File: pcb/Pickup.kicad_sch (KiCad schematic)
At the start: 39 parts, among them IC1 MAX9924UAUB+, K1 AQY212EHAX, Q7 MMBT2222A, T1 SM-LP-5001E

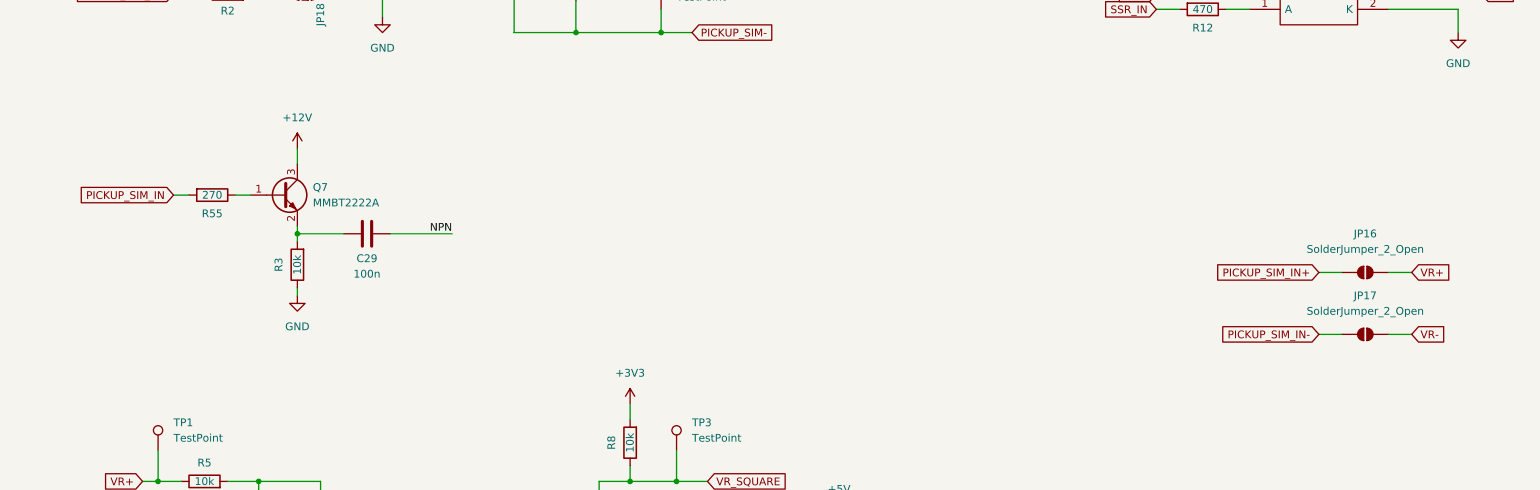
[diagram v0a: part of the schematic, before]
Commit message: simplified pickup simulation pinout
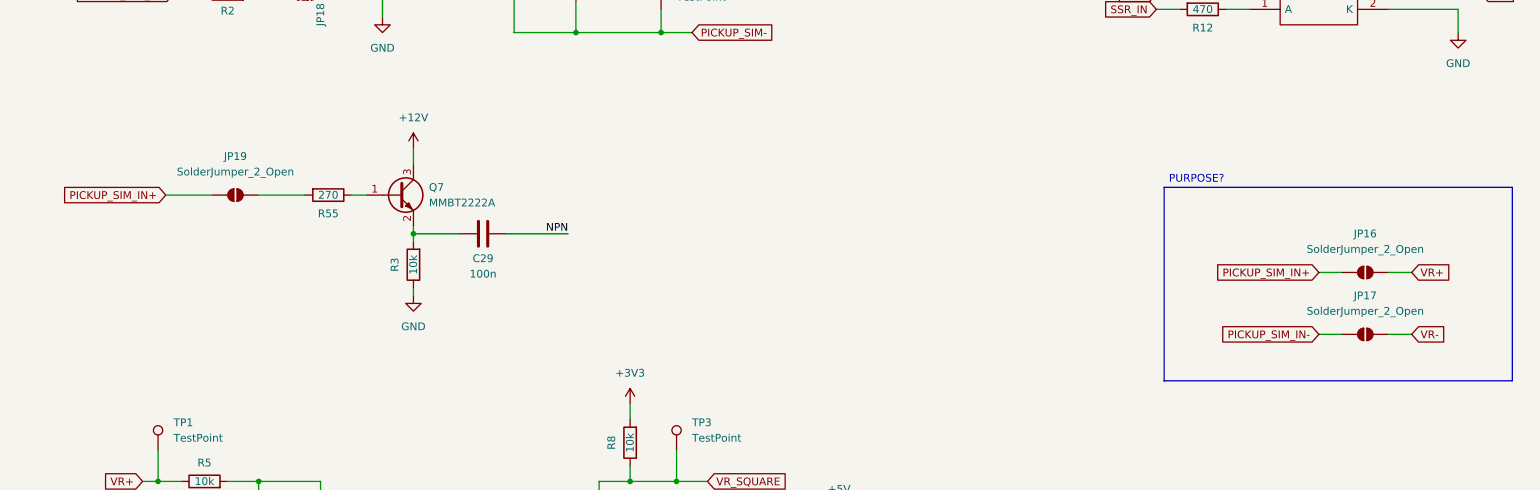
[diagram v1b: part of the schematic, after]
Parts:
- added JP19: SolderJumper_2_Open, Jumper:SolderJumper-2_P1.3mm_Open_RoundedPad1.0x1.5mm, symbol Jumper:SolderJumper_2_Open
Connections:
- net PICKUP_SIM_IN+: now also JP19.2 (B)
- net PICKUP_SIM_IN: no longer names the net of R55.2
- net PICKUP_SIM_IN: now also JP19.1 (A)
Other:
- note added: "PURPOSE?"
- moved on the sheet: C29, Q7, R3, R55

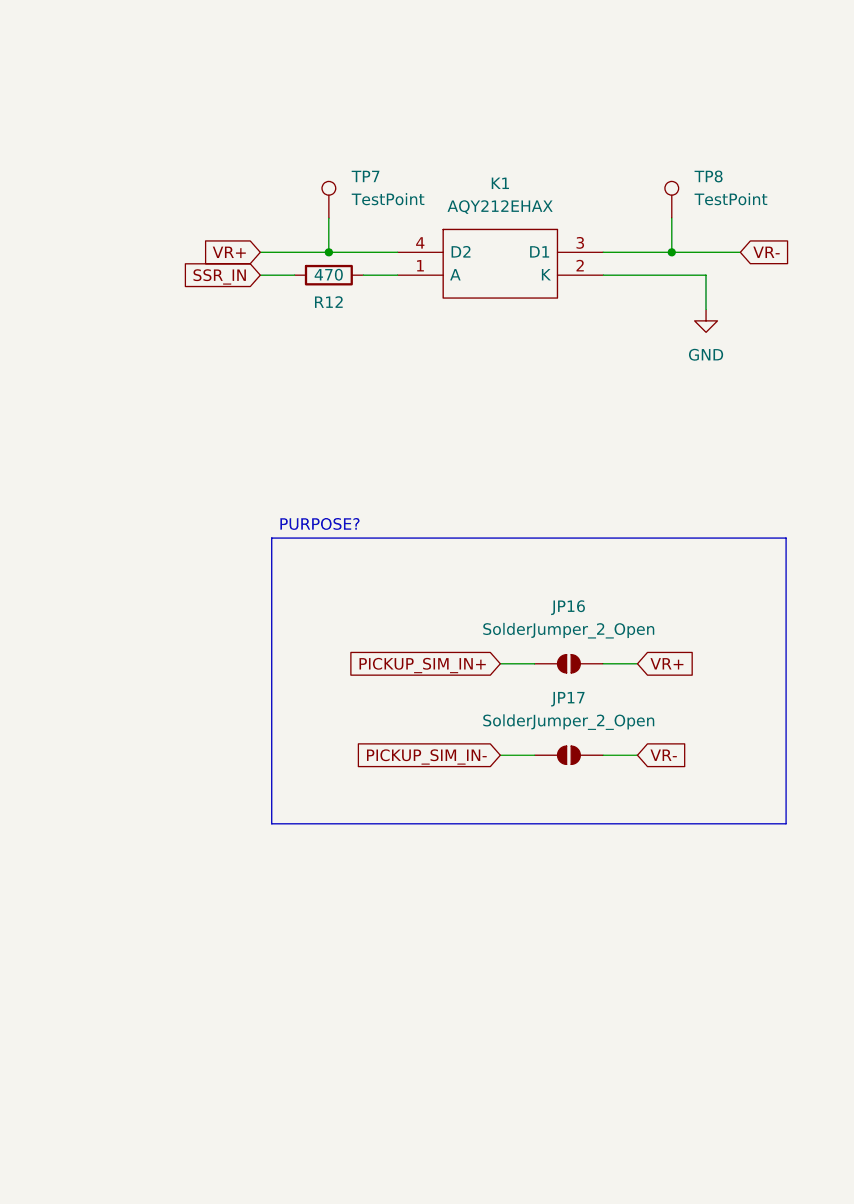
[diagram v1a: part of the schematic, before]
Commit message: completed photomos revision
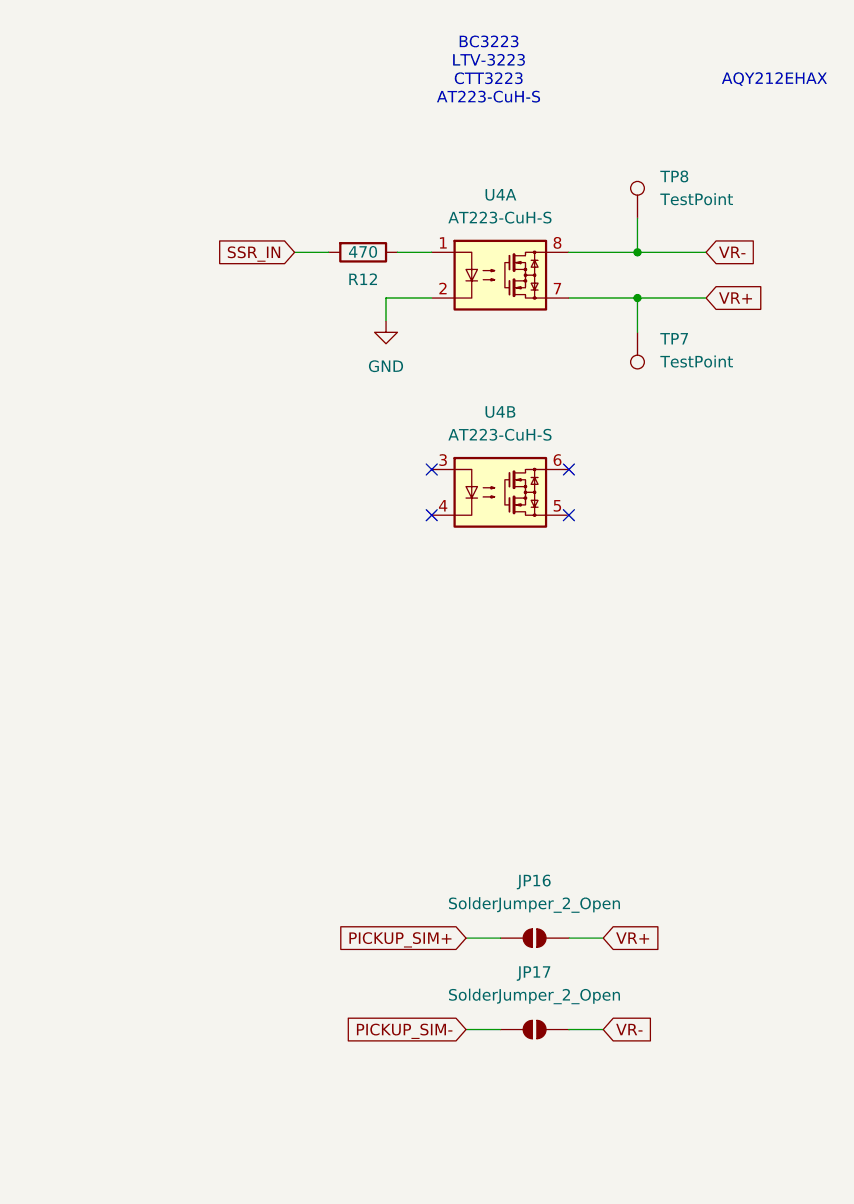
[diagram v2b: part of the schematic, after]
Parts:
- removed K1: AQY212EHAX, SamacSys_Parts:AQY212EHAX, symbol SamacSys_Parts:AQY212EHAX
- added U4: AT223-CuH-S, Package_SO:SOIC-8_5.3x5.3mm_P1.27mm, symbol Relay_SolidState:CPC2125N
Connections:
- net GND: now also U4.2
- net PICKUP_SIM+: now also JP16.2 (B)
- net PICKUP_SIM-: now also JP17.2 (B)
- net PICKUP_SIM_IN+: no longer JP16.2 (B)
- net PICKUP_SIM_IN-: no longer JP17.2 (B)
- net VR+: now also U4.7
- net VR-: now also U4.8
- net at R12.1: now also U4.1
- no-connect marks 2 -> 6
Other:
- note added: "AQY212EHAX"
- note added: "BC3223 LTV-3223 CTT3223 AT223-CuH-S"
- note removed: "PURPOSE?"
- moved on the sheet: JP16, JP17, R12, TP7, TP8

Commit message: changed photomos footprint to match datasheet
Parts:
- U4: footprint Package_SO:SOIC-8_5.3x5.3mm_P1.27mm -> Package_SO:SOP-8_6.605x9.655mm_P2.54mm
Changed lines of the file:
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@@
 			)
 		)
-		(property "Footprint" "Package_SO:SOIC-8_5.3x5.3mm_P1.27mm"
+		(property "Footprint" "Package_SO:SOP-8_6.605x9.655mm_P2.54mm"
 			(at 229.87 77.47 0)
 			(effects
@@
 			)
 		)
-		(property "Footprint" "Package_SO:SOIC-8_5.3x5.3mm_P1.27mm"
+		(property "Footprint" "Package_SO:SOP-8_6.605x9.655mm_P2.54mm"
 			(at 229.87 53.34 0)
 			(effects

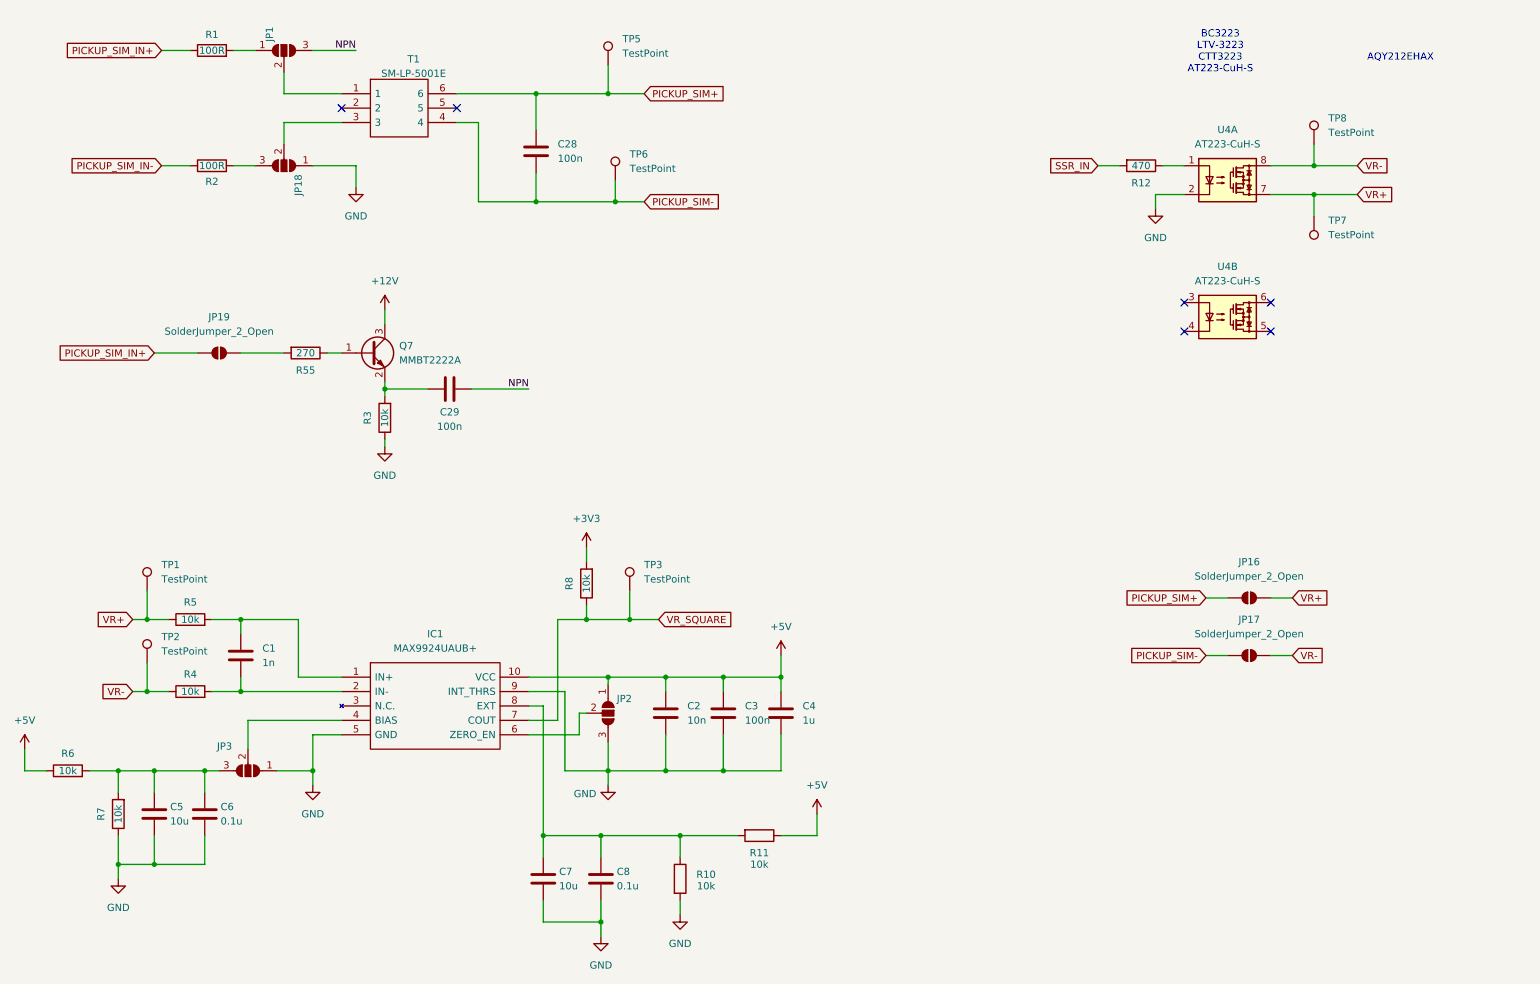
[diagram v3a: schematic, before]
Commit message: added DNP for fabrication and 2P molex connector, minor fixes
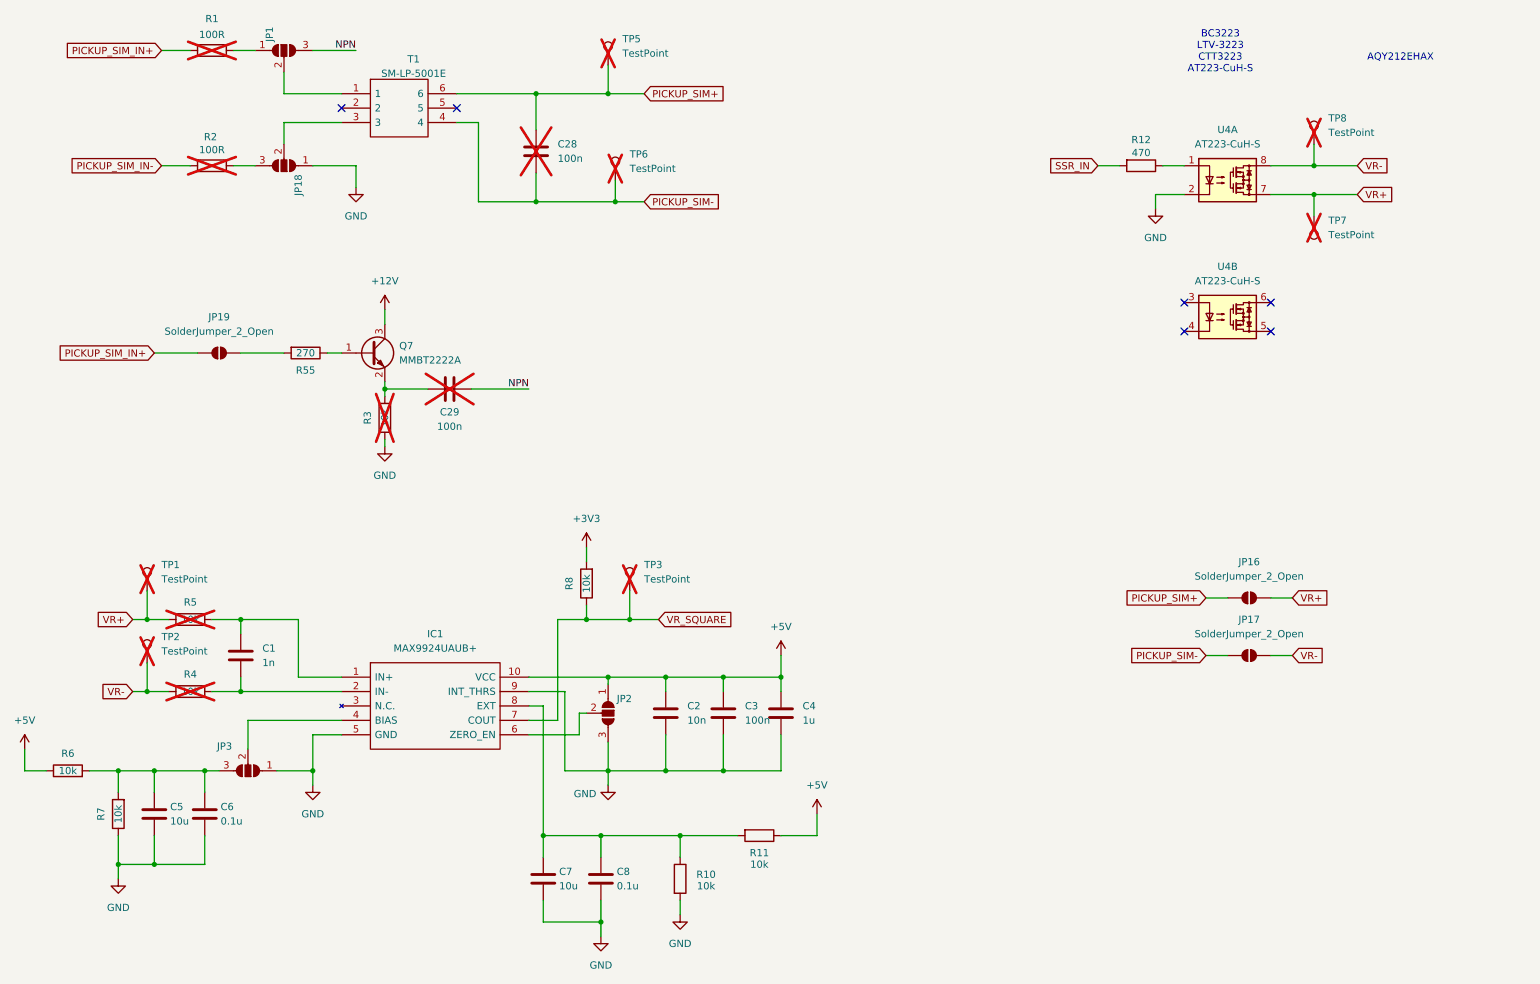
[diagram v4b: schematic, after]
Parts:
- C28, C29, R1, R2, R3, R4, R5: now not fitted
- TP1, TP2, TP3, TP5, TP6, TP7, TP8: footprint Connector_PinHeader_1.00mm:PinHeader_1x01_P1.00mm_Vertical -> Connector_PinHeader_2.54mm:PinHeader_1x01_P2.54mm_Vertical; now not fitted
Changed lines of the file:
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@@
 		(in_bom yes)
 		(on_board yes)
-		(dnp no)
+		(dnp yes)
 		(fields_autoplaced yes)
 		(property "Reference" "TP5"
@@
 			)
 		)
-		(property "Footprint" "Connector_PinHeader_1.00mm:PinHeader_1x01_P1.00mm_Vertical"
+		(property "Footprint" "Connector_PinHeader_2.54mm:PinHeader_1x01_P2.54mm_Vertical"
 			(at 125.73 27.94 0)
 			(effects
@@
 		(in_bom yes)
 		(on_board yes)
-		(dnp no)
+		(dnp yes)
 		(fields_autoplaced yes)
 		(property "Reference" "TP1"
@@
 			)
 		)
-		(property "Footprint" "Connector_PinHeader_1.00mm:PinHeader_1x01_P1.00mm_Vertical"
+		(property "Footprint" "Connector_PinHeader_2.54mm:PinHeader_1x01_P2.54mm_Vertical"
 			(at 44.45 120.65 0)
 			(effects
@@
 		(in_bom yes)
 		(on_board yes)
-		(dnp no)
+		(dnp yes)
 		(property "Reference" "TP7"
 			(at 247.65 55.372 0)
@@
 			)
 		)
-		(property "Footprint" "Connector_PinHeader_1.00mm:PinHeader_1x01_P1.00mm_Vertical"
+		(property "Footprint" "Connector_PinHeader_2.54mm:PinHeader_1x01_P2.54mm_Vertical"
 			(at 240.03 54.61 0)
 			(effects
@@
 		(dnp no)
 		(property "Reference" "R12"
-			(at 214.63 48.768 90)
+			(at 214.63 41.148 90)
 			(effects
 				(font
@@
 		)
 		(property "Value" "470"
-			(at 214.63 45.72 90)
+			(at 214.63 43.434 90)
 			(effects
 				(font
@@
 		(in_bom yes)
 		(on_board yes)
-		(dnp no)
+		(dnp yes)
 		(fields_autoplaced yes)
 		(property "Reference" "TP3"
@@
 			)
 		)
-		(property "Footprint" "Connector_PinHeader_1.00mm:PinHeader_1x01_P1.00mm_Vertical"
+		(property "Footprint" "Connector_PinHeader_2.54mm:PinHeader_1x01_P2.54mm_Vertical"
 			(at 129.54 120.65 0)
 			(effects
@@
 		(in_bom yes)
 		(on_board yes)
-		(dnp no)
+		(dnp yes)
 		(property "Reference" "R1"
-			(at 50.8 22.606 90)
+			(at 50.8 19.812 90)
 			(effects
 				(font
@@
 		)
 		(property "Value" "100R"
-			(at 50.8 25.4 90)
+			(at 50.8 22.606 90)
 			(effects
 				(font
@@
 		(in_bom yes)
 		(on_board yes)
-		(dnp no)
+		(dnp yes)
 		(fields_autoplaced yes)
 		(property "Reference" "C28"
@@
 		(in_bom yes)
 		(on_board yes)
-		(dnp no)
+		(dnp yes)
 		(property "Reference" "R2"
-			(at 50.8 48.514 90)
+			(at 50.546 40.64 90)
 			(effects
 				(font
@@
 		)
 		(property "Value" "100R"
-			(at 50.8 45.72 90)
+			(at 50.8 42.926 90)
 			(effects
 				(font
@@
 		(in_bom yes)
 		(on_board yes)
-		(dnp no)
+		(dnp yes)
 		(fields_autoplaced yes)
 		(property "Reference" "TP8"
@@
 			)
 		)
-		(property "Footprint" "Connector_PinHeader_1.00mm:PinHeader_1x01_P1.00mm_Vertical"
+		(property "Footprint" "Connector_PinHeader_2.54mm:PinHeader_1x01_P2.54mm_Vertical"
 			(at 250.19 41.91 0)
 			(effects
@@
 		(in_bom yes)
 		(on_board yes)
-		(dnp no)
+		(dnp yes)
 		(property "Reference" "C29"
 			(at 92.71 89.154 90)
@@
 		(in_bom yes)
 		(on_board yes)
-		(dnp no)
+		(dnp yes)
 		(fields_autoplaced yes)
 		(property "Reference" "TP6"
@@
 			)
 		)
-		(property "Footprint" "Connector_PinHeader_1.00mm:PinHeader_1x01_P1.00mm_Vertical"
+		(property "Footprint" "Connector_PinHeader_2.54mm:PinHeader_1x01_P2.54mm_Vertical"
 			(at 127 48.26 0)
 			(effects
@@
 		(in_bom yes)
 		(on_board yes)
-		(dnp no)
+		(dnp yes)
 		(property "Reference" "R5"
 			(at 46.99 122.682 90)
@@
 		(in_bom yes)
 		(on_board yes)
-		(dnp no)
+		(dnp yes)
 		(fields_autoplaced yes)
 		(property "Reference" "TP2"
@@
 			)
 		)
-		(property "Footprint" "Connector_PinHeader_1.00mm:PinHeader_1x01_P1.00mm_Vertical"
+		(property "Footprint" "Connector_PinHeader_2.54mm:PinHeader_1x01_P2.54mm_Vertical"
 			(at 44.45 133.35 0)
 			(effects
@@
 		(in_bom yes)
 		(on_board yes)
-		(dnp no)
+		(dnp yes)
 		(property "Reference" "R4"
 			(at 46.99 135.382 90)
@@
 		(in_bom yes)
 		(on_board yes)
-		(dnp no)
+		(dnp yes)
 		(property "Reference" "R3"
 			(at 78.232 90.17 90)
